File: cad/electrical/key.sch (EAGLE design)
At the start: 12 parts, among them Q1 PSMN022-30PL, U1 LD1117V50, U2 LM2903N

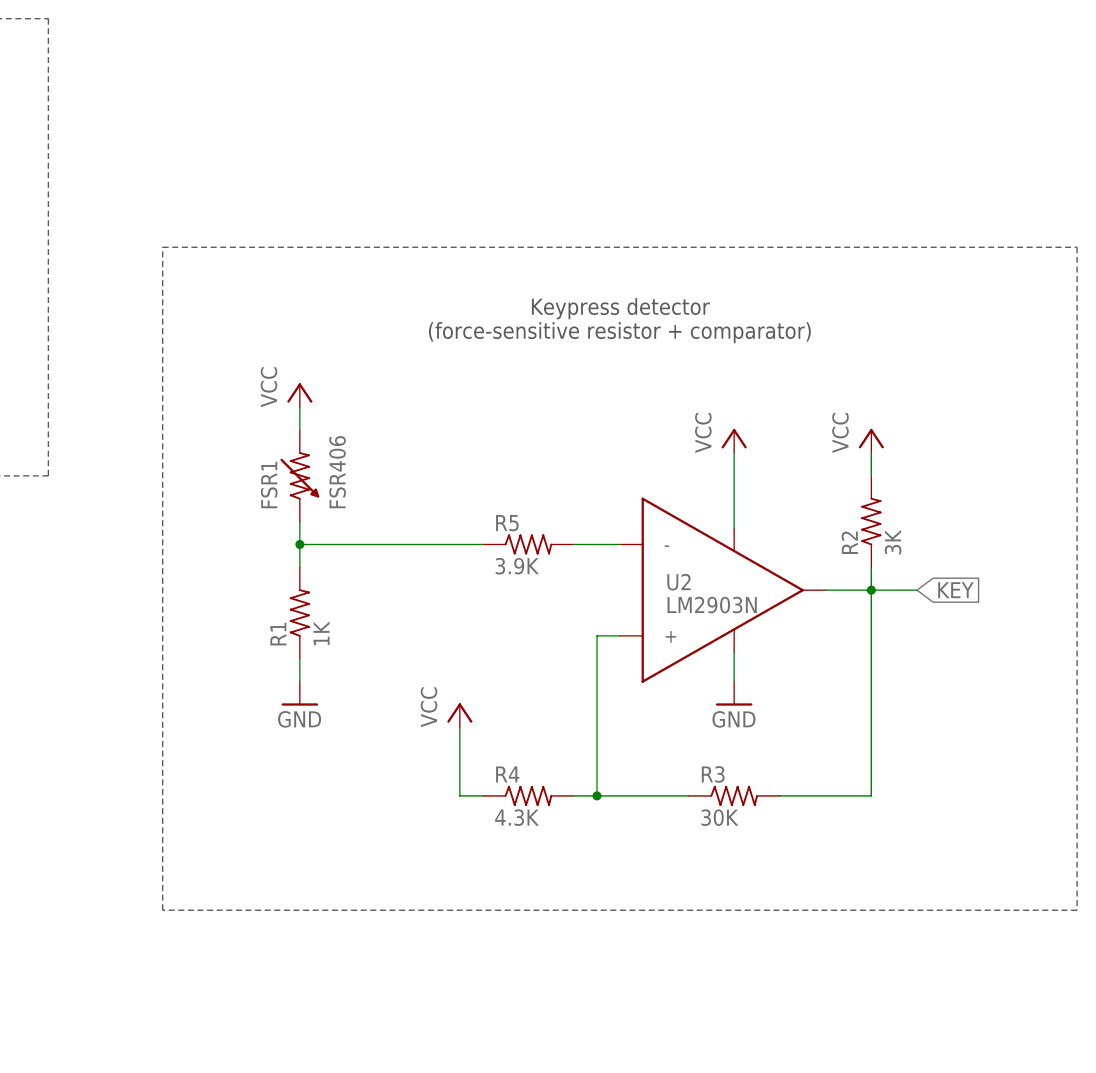
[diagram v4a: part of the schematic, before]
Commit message: Adjusted voltage divider to limit current through FSR to 1mA
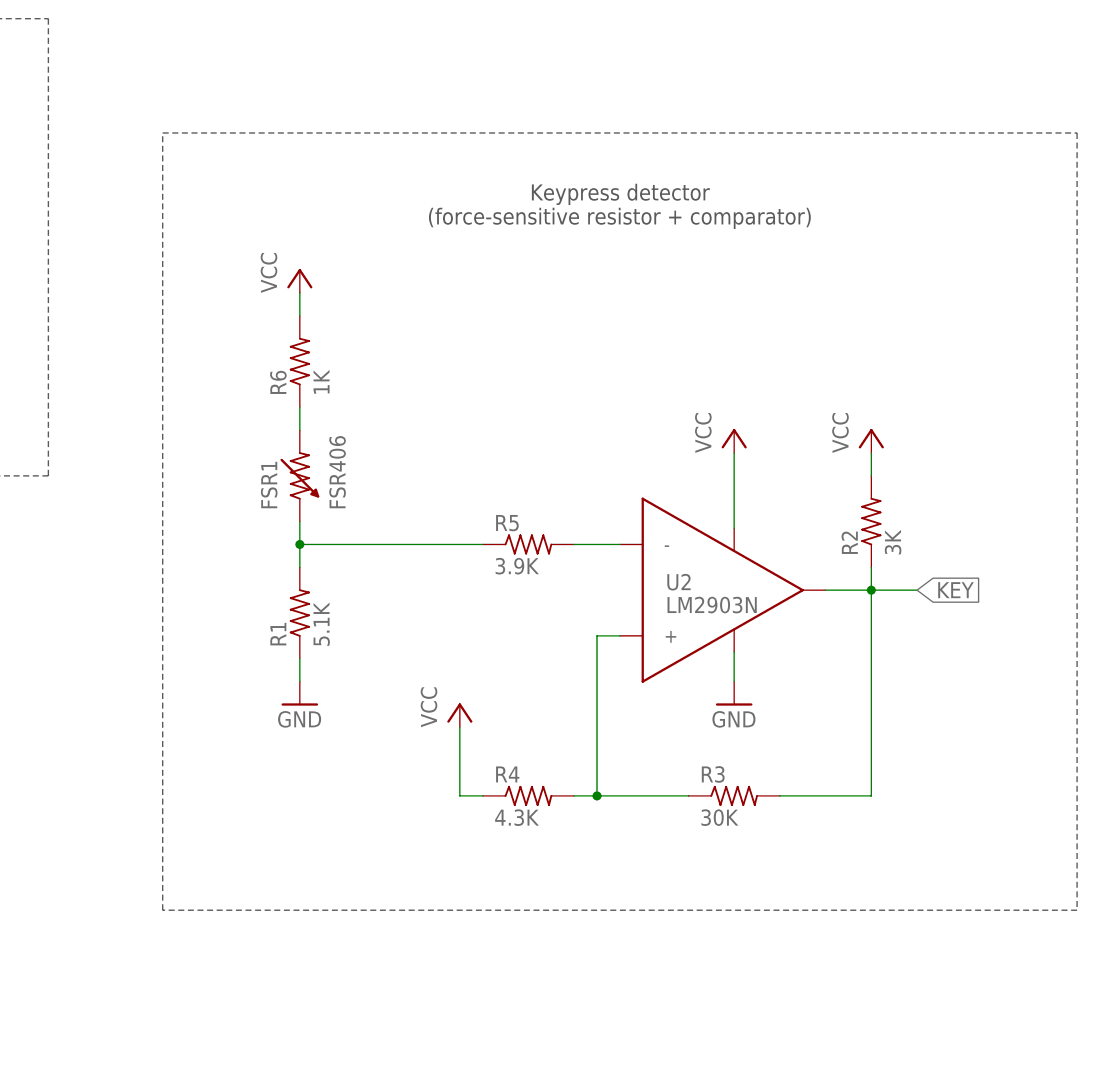
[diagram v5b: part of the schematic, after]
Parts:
- added R6: 1K, rcl:R-US_0207/10
- R1: value 1K -> 5.1K
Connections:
- new net N$1: FSR1.2, R6.1
- net VCC: now also R6.2; no longer FSR1.2
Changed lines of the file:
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@@
 <part name="GND2" library="supply1" deviceset="GND" device=""/>
 <part name="P+3" library="supply1" deviceset="VCC" device=""/>
-<part name="R1" library="rcl" deviceset="R-US_" device="0207/10" value="1K"/>
+<part name="R1" library="rcl" deviceset="R-US_" device="0207/10" value="5.1K"/>
 <part name="U2" library="my-custom" deviceset="LM2903P" device="" value="LM2903N"/>
 <part name="P+4" library="supply1" deviceset="VCC" device=""/>
@@
 <part name="JP1" library="pinhead" deviceset="PINHD-1X2" device="/90" value="LED STRIP"/>
 <part name="P+7" library="supply1" deviceset="+12V" device=""/>
+<part name="R6" library="rcl" deviceset="R-US_" device="0207/10" value="1K"/>
 </parts>
 <sheets>
@@
 <wire x1="38.1" y1="109.22" x2="38.1" y2="160.02" width="0.1524" layer="97" style="longdash"/>
 <text x="76.2" y="152.4" size="1.778" layer="97" align="bottom-center">Power supply</text>
-<wire x1="127" y1="134.62" x2="228.6" y2="134.62" width="0.1524" layer="97" style="longdash"/>
-<wire x1="228.6" y1="134.62" x2="228.6" y2="60.96" width="0.1524" layer="97" style="longdash"/>
+<wire x1="127" y1="147.32" x2="228.6" y2="147.32" width="0.1524" layer="97" style="longdash"/>
+<wire x1="228.6" y1="147.32" x2="228.6" y2="60.96" width="0.1524" layer="97" style="longdash"/>
 <wire x1="228.6" y1="60.96" x2="127" y2="60.96" width="0.1524" layer="97" style="longdash"/>
-<wire x1="127" y1="60.96" x2="127" y2="134.62" width="0.1524" layer="97" style="longdash"/>
-<text x="177.8" y="124.46" size="1.778" layer="97" align="bottom-center">Keypress detector
+<wire x1="127" y1="60.96" x2="127" y2="147.32" width="0.1524" layer="97" style="longdash"/>
+<text x="177.8" y="137.16" size="1.778" layer="97" align="bottom-center">Keypress detector
 (force-sensitive resistor + comparator)</text>
 <wire x1="48.26" y1="93.98" x2="104.14" y2="93.98" width="0.1524" layer="97" style="longdash"/>
@@
 <instance part="GND1" gate="1" x="76.2" y="119.38"/>
 <instance part="GND2" gate="1" x="142.24" y="83.82"/>
-<instance part="P+3" gate="VCC" x="142.24" y="119.38"/>
+<instance part="P+3" gate="VCC" x="142.24" y="132.08"/>
 <instance part="R1" gate="G$1" x="142.24" y="93.98" rot="R90"/>
 <instance part="U2" gate="G$1" x="180.34" y="96.52"/>
@@
 <instance part="JP1" gate="G$1" x="86.36" y="60.96"/>
 <instance part="P+7" gate="1" x="76.2" y="73.66"/>
+<instance part="R6" gate="G$1" x="142.24" y="121.92" rot="R90"/>
 </instances>
 <busses>
@@
 <nets>
 <net name="VCC" class="0">
-<segment>
-<pinref part="P+3" gate="VCC" pin="VCC"/>
-<pinref part="FSR1" gate="G$1" pin="2"/>
-<wire x1="142.24" y1="116.84" x2="142.24" y2="114.3" width="0.1524" layer="91"/>
-</segment>
 <segment>
 <pinref part="P+4" gate="VCC" pin="VCC"/>
@@
 <wire x1="162.56" y1="73.66" x2="160.02" y2="73.66" width="0.1524" layer="91"/>
 <wire x1="160.02" y1="73.66" x2="160.02" y2="81.28" width="0.1524" layer="91"/>
+</segment>
+<segment>
+<pinref part="R6" gate="G$1" pin="2"/>
+<pinref part="P+3" gate="VCC" pin="VCC"/>
+<wire x1="142.24" y1="127" x2="142.24" y2="129.54" width="0.1524" layer="91"/>
 </segment>
 </net>
@@
 </segment>
 </net>
+<net name="N$1" class="0">
+<segment>
+<pinref part="R6" gate="G$1" pin="1"/>
+<pinref part="FSR1" gate="G$1" pin="2"/>
+<wire x1="142.24" y1="116.84" x2="142.24" y2="114.3" width="0.1524" layer="91"/>
+</segment>
+</net>
